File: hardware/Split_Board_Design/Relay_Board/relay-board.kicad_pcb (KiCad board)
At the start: 4 copper layers, 100 x 60 mm, 19 parts, among them J5 XT60PW-M, J6 Conn_01x06, J7 XT60PW-M, Q7 MJD41CT4G, U13 LTV-356T, U8 HF116F-80/24-1HTF

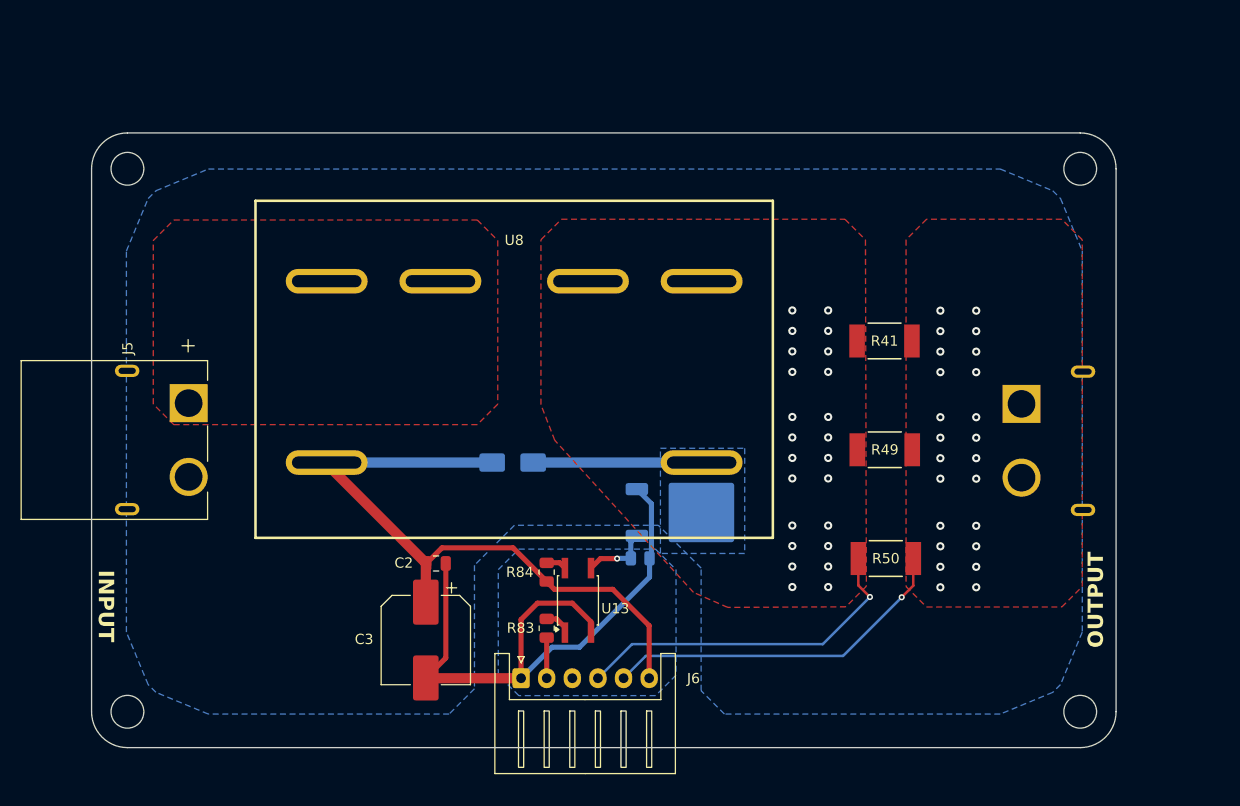
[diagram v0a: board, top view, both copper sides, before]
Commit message: feat(layout): Finish demo layout of relay board
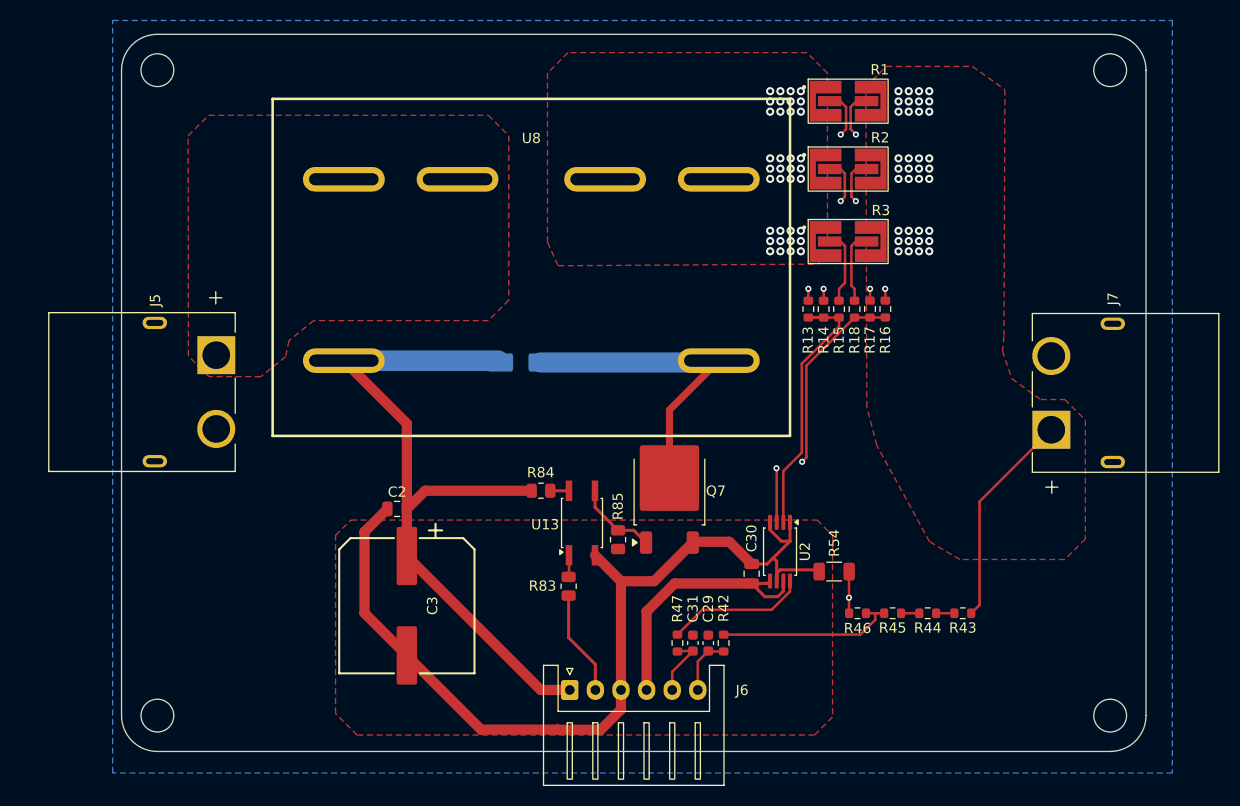
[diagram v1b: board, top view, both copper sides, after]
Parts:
- removed R41, R49, R50: 2mR, RobotChargeController:RES_1L00x_BRN
- added C29: 100nF-50V, Capacitor_SMD:C_0603_1608Metric, F.Cu at (158.3, 117.4)
- added C30: 100nF, Capacitor_SMD:C_0805_2012Metric, F.Cu at (162.5, 110.7)
- added C31: 10nF-50V, Capacitor_SMD:C_0603_1608Metric, F.Cu at (156.8, 117.4)
- added R1: 2mR, RobotChargeController:R_Shunt_FOJAN_2512L_4Terminal_Kelvin_C, F.Cu at (171.9, 64.5)
- added R13: 1R, Resistor_SMD:R_0603_1608Metric, F.Cu at (168.0, 84.8)
- added R14: 1R, Resistor_SMD:R_0603_1608Metric, F.Cu at (169.5, 84.8)
- added R15: 1R, Resistor_SMD:R_0603_1608Metric, F.Cu at (171.0, 84.8)
- added R16: 1R, Resistor_SMD:R_0603_1608Metric, F.Cu at (175.6, 84.8)
- added R17: 1R, Resistor_SMD:R_0603_1608Metric, F.Cu at (174.1, 84.8)
- added R18: 1R, Resistor_SMD:R_0603_1608Metric, F.Cu at (172.6, 84.8)
- added R2: 2mR, RobotChargeController:R_Shunt_FOJAN_2512L_4Terminal_Kelvin_C, F.Cu at (171.9, 71.2)
- added R3: 2mR, RobotChargeController:R_Shunt_FOJAN_2512L_4Terminal_Kelvin_C, F.Cu at (171.9, 78.2)
- added R42: 10kR, Resistor_SMD:R_0603_1608Metric, F.Cu at (159.8, 117.4)
- added R43: 150kR, Resistor_SMD:R_0603_1608Metric, F.Cu at (183.1, 114.5)
- added R44: 150kR, Resistor_SMD:R_0603_1608Metric, F.Cu at (179.7, 114.5)
- added R45: 150kR, Resistor_SMD:R_0603_1608Metric, F.Cu at (176.3, 114.5)
- added R46: 18kR, Resistor_SMD:R_0603_1608Metric, F.Cu at (172.8, 114.5)
- added R47: 1kR, Resistor_SMD:R_0603_1608Metric, F.Cu at (155.3, 117.4)
- added R54: 0R, Resistor_SMD:R_1206_3216Metric, F.Cu at (170.6, 110.4)
- added U2: INA240A2PW, Package_SO:TSSOP-8_4.4x3mm_P0.65mm, F.Cu at (165.3, 108.5)
- C3: value 100uF-50V -> 680uf-35v; footprint Capacitor_SMD:CP_Elec_8x10.5 -> RobotChargeController:CP_Elec_12.5x13.5_Generic_H13
- J7, Q7, R85: moved to F.Cu
- moved H4 109.8 mm to (197.5, 124.5)
- moved H5 90.6 mm to (104.5, 61.5)
- moved H6 62.7 mm to (197.5, 61.5)
- moved U8 10.1 mm to (141.0, 81.0)
- moved D7 9.80 mm to (140.0, 90.0)
- moved R84 7.97 mm to (141.9, 102.5), turned to 180 degrees
- moved U13 7.56 mm to (145.9, 105.7)
- moved C2 6.54 mm to (127.9, 104.3), turned to 180 degrees
- moved J7 5.50 mm to (197.8, 93.0), turned to 90 degrees
- moved J5 5.40 mm to (104.2, 92.9)
- moved J6 4.89 mm to (144.8, 122.0)
- moved R83 4.63 mm to (144.6, 111.9)
- moved C3 3.83 mm to (128.8, 113.8)
- moved H7 2.95 mm to (104.5, 124.5)
- moved R85 2.83 mm to (149.5, 107.3), turned to 90 degrees
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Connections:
- J6 pad 1: GND -> +24V
- J6 pad 3: 60V_GND -> GND
- J6 pad 4: /Relay_control/VBAT_RELAY_OUT_P -> +3V3
- J6 pad 5: Net-(J6-Pin_5) -> /Output_Sensing/IOUT_SENSE_ADC
- J6 pad 6: +24V -> /Output_Sensing/VOUT_SENSE_ADC
- J7 pad 1: Net-(J6-Pin_5) -> /Output_Sensing/VBAT_SEN_OUT_P
- U8 pad 6: /Relay_control/VBAT_RELAY_OUT_P -> /Output_Sensing/VBAT_RELAY_OUT_P
- U8 pad 8: /Relay_control/VBAT_RELAY_OUT_P -> /Output_Sensing/VBAT_RELAY_OUT_P
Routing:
- net /Relay_control/VBAT_RELAY_OUT_P: track 45.2 -> 0.00 mm, vias 25 -> 0
- net Net-(J6-Pin_5): track 34.7 -> 0.00 mm, vias 25 -> 0
- net GND: track 62.2 -> 90.2 mm
- net Net-(U2--): track 0.00 -> 27.3 mm, vias 0 -> 2
- net Net-(U2-+): track 0.00 -> 26.7 mm
- net +3V3: track 0.00 -> 25.8 mm
- net Net-(R1-V_A): track 0.00 -> 22.2 mm, vias 0 -> 2
- net Net-(R1-V_B): track 0.00 -> 22.1 mm, vias 0 -> 2
- net /Output_Sensing/VBAT_SEN_OUT_P: track 0.00 -> 21.2 mm, vias 0 -> 36
- net Net-(R42-Pad2): track 0.00 -> 17.8 mm
- net Net-(R2-V_A): track 0.00 -> 15.2 mm, vias 0 -> 2
- net Net-(R2-V_B): track 0.00 -> 15.1 mm, vias 0 -> 2
- net Net-(D7-A): track 16.4 -> 30.9 mm
- net Net-(R47-Pad2): track 0.00 -> 13.7 mm
- net Net-(R3-V_A): track 0.00 -> 7.20 mm
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- added copper zone on F.Cu, net /Output_Sensing/VBAT_RELAY_OUT_P
- added copper zone on In2.Cu, net /Output_Sensing/VBAT_RELAY_OUT_P
- added copper zone on F.Cu, net /Output_Sensing/VBAT_SEN_OUT_P
- added copper zone on In2.Cu, net /Output_Sensing/VBAT_SEN_OUT_P
- added copper zone on F.Cu, net GND
- removed copper zone on F.Cu, net /Relay_control/VBAT_RELAY_OUT_P
- removed copper zone on In2.Cu, net /Relay_control/VBAT_RELAY_OUT_P
- removed copper zone on B.Cu, net GND
- removed copper zone on B.Cu, net Net-(D7-A)
- removed copper zone on F.Cu, net Net-(J6-Pin_5)
- removed copper zone on In2.Cu, net Net-(J6-Pin_5)
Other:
- board size 100 x 60 mm -> 100 x 70 mm
- board text added: "{ "ViaStitching": "0.3.0", "stitch_zone_0": { "HSpacing": "1", "VSpacing": "1", "HOffset": "0", "VOffset": "0", "Clearance": "0.5", "Randomize": false, "Stagger": false, "OnlyFilledCopper": true } }"
- board text removed: "INPUT"
- board text removed: "OUTPUT"

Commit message: delete junk files
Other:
- board text added: "INPUT"
- board text added: "OUTPUT"

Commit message: feat(layout): Update layout
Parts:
- removed R13, R14, R15, R16, R17, R18: 1R, Resistor_SMD:R_0603_1608Metric
- C30: value 100nF -> 100nF-50V
- moved C3 4.98 mm to (133.6, 115.3), turned to 0 degrees
- moved R83 4.08 mm to (144.6, 115.9)
- moved R84 4.08 mm to (141.9, 106.6)
- moved U13 4.08 mm to (145.9, 109.8)
- moved C2 3.49 mm to (129.7, 107.3), turned to 0 degrees
- moved R3 2.40 mm to (171.9, 75.8)
- moved R1 1.95 mm to (172.0, 66.5)
- moved R85 0.28 mm to (149.4, 107.0)
- moved U2 0.15 mm to (165.3, 108.7)
- moved C30 0.09 mm to (162.4, 110.6)
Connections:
- R1 pad 3: Net-(R1-V_A) -> /Output_Sensing/VBAT_RELAY_OUT_P
- R1 pad 4: Net-(R1-V_B) -> /Output_Sensing/VBAT_SEN_OUT_P
- R2 pad 3: Net-(R2-V_A) -> /Output_Sensing/VBAT_RELAY_OUT_P
- R2 pad 4: Net-(R2-V_B) -> /Output_Sensing/VBAT_SEN_OUT_P
- R3 pad 3: Net-(R3-V_A) -> /Output_Sensing/VBAT_RELAY_OUT_P
- R3 pad 4: Net-(R3-V_B) -> /Output_Sensing/VBAT_SEN_OUT_P
- U2 pad 2: Net-(U2-+) -> /Output_Sensing/VBAT_RELAY_OUT_P
- U2 pad 3: Net-(U2--) -> /Output_Sensing/VBAT_SEN_OUT_P
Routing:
- net GND: track 90.2 -> 0.00 mm
- net /Output_Sensing/VBAT_SEN_OUT_P: track 21.2 -> 61.2 mm, vias 36 -> 38
- net /Output_Sensing/VBAT_RELAY_OUT_P: track 0.00 -> 38.4 mm
- net Net-(U2--): track 27.3 -> 0.00 mm, vias 2 -> 0
- net Net-(U2-+): track 26.7 -> 0.00 mm
- net Net-(R1-V_A): track 22.2 -> 0.00 mm, vias 2 -> 0
- net Net-(R1-V_B): track 22.1 -> 0.00 mm, vias 2 -> 0
- net Net-(R2-V_A): track 15.2 -> 0.00 mm, vias 2 -> 0
- net Net-(R2-V_B): track 15.1 -> 0.00 mm, vias 2 -> 0
- net Net-(R3-V_A): track 7.20 -> 0.00 mm
- net Net-(R3-V_B): track 7.11 -> 0.00 mm
- net +24V: track 71.2 -> 76.9 mm
- net /Relay_control/MAIN_RELAY_EN: track 10.3 -> 6.23 mm
- net Net-(Q7-B): track 8.03 -> 5.83 mm
- net /Output_Sensing/IOUT_SENSE_ADC: track 6.17 -> 5.47 mm

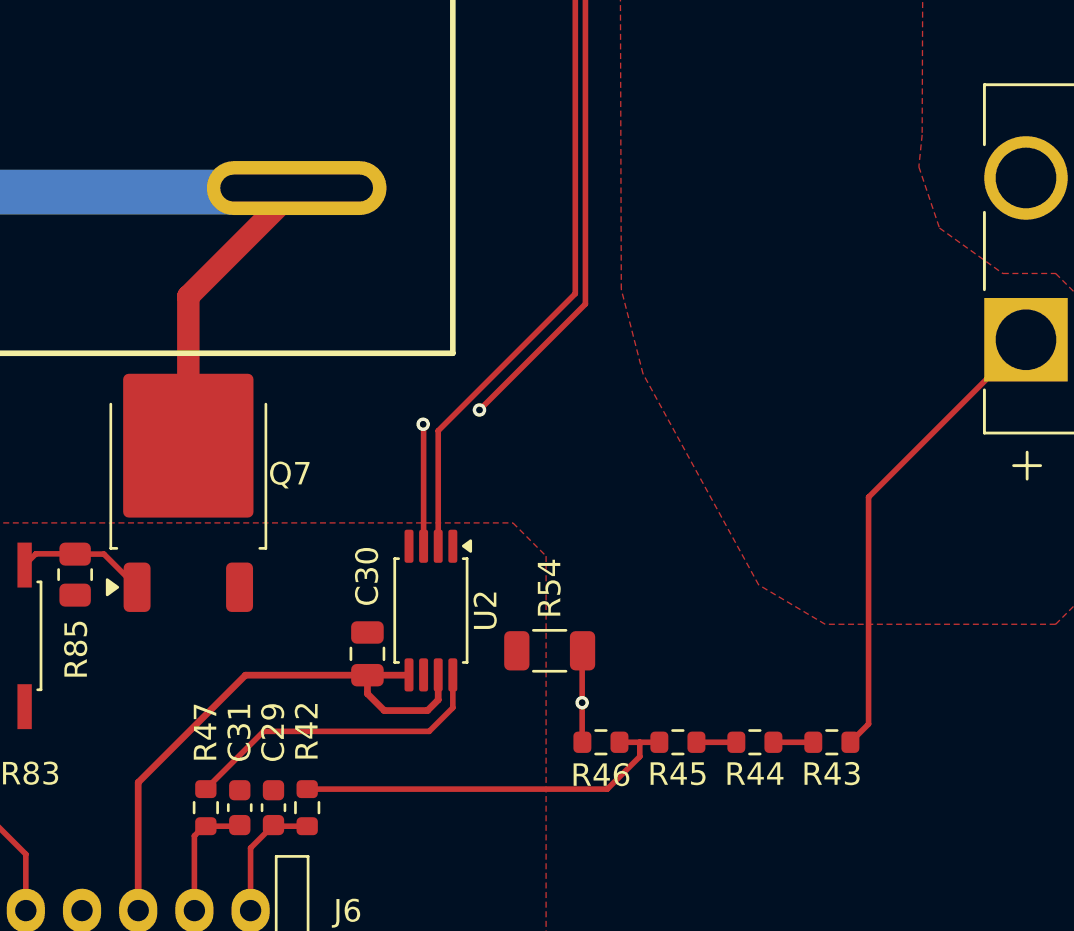
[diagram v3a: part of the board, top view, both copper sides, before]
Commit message: feat(schematic): update INA240A2PW to ÍNA240A2D
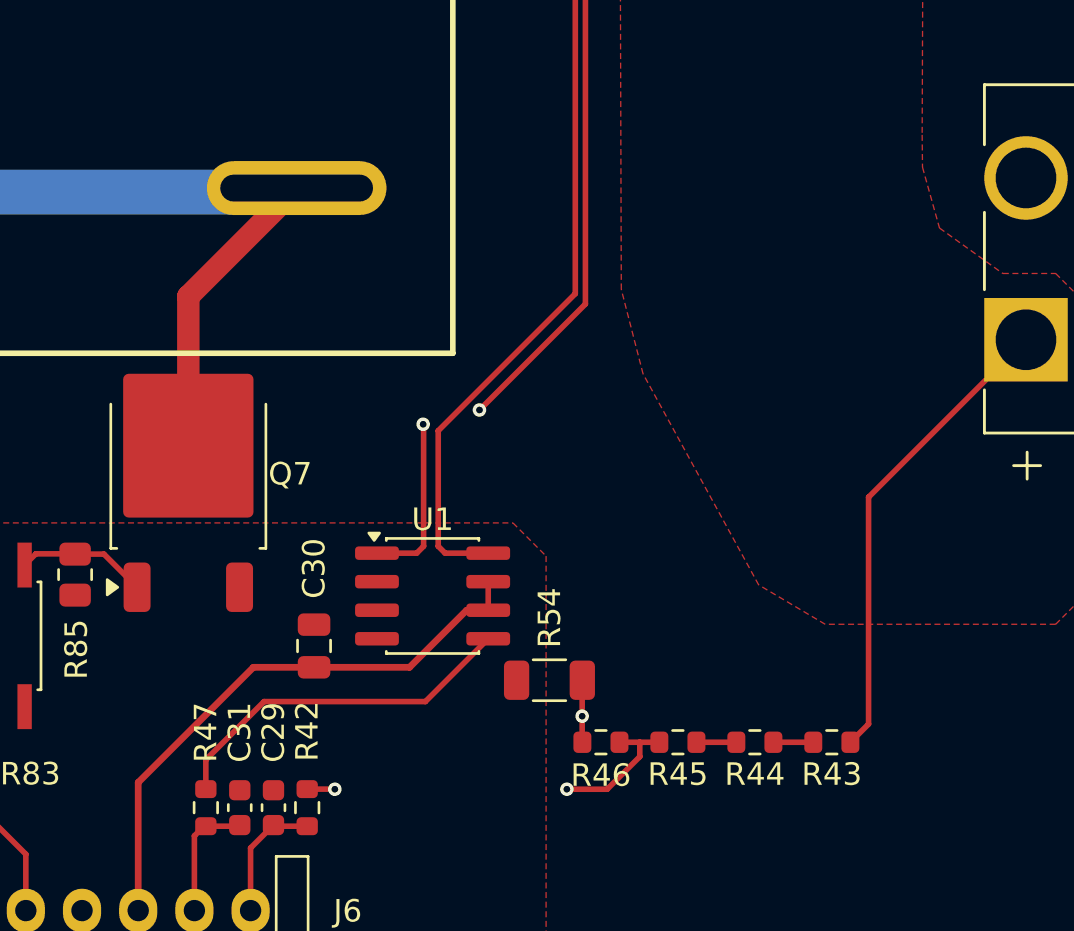
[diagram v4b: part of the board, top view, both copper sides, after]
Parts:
- removed U2: INA240A2PW, Package_SO:TSSOP-8_4.4x3mm_P0.65mm
- added U1: INA240A2D, Package_SO:SOIC-8_3.9x4.9mm_P1.27mm, F.Cu at (165.3, 108.0)
- moved C30 2.40 mm to (160.1, 110.2)
- moved R54 1.31 mm to (170.6, 111.8)
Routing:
- net /Output_Sensing/VBAT_RELAY_OUT_P: track 38.4 -> 40.8 mm
- net /Output_Sensing/VBAT_SEN_OUT_P: track 61.2 -> 63.4 mm
- net Net-(R47-Pad2): track 14.0 -> 16.1 mm
- net 60V_GND: track 4.08 -> 2.77 mm
- net Net-(R42-Pad2): vias 0 -> 2

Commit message: feat(layout): update relay board layout
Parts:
- removed C2: 100nF-50V, Capacitor_SMD:C_0805_2012Metric
- removed R1, R2, R3: 2mR, RobotChargeController:R_Shunt_FOJAN_2512L_4Terminal_Kelvin_C
- added J3: XT30PW-M, RobotChargeController:AMASS_XT30PW-M, F.Cu at (102.9, 109.5)
- added R48: 2mR, RobotChargeController:R_Shunt_FOJAN_2512L_4Terminal_Kelvin_C, F.Cu at (172.1, 66.4)
- added R49: 2mR, RobotChargeController:R_Shunt_FOJAN_2512L_4Terminal_Kelvin_C, F.Cu at (172.0, 71.2)
- added R50: 2mR, RobotChargeController:R_Shunt_FOJAN_2512L_4Terminal_Kelvin_C, F.Cu at (172.1, 75.8)
- C31: value 10nF-50V -> 100nF-50V
- R42: value 10kR -> 1kR
- moved C3 11.6 mm to (122.0, 116.8), turned to -90 degrees
- moved J5 9.83 mm to (104.3, 83.1)
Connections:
- J6 pad 1: +24V -> unconnected-(J6-Pin_1-Pad1)
- J6 pad 3: GND -> unconnected-(J6-Pin_3-Pad3)
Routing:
- net GND: track 0.00 -> 41.3 mm
- net +24V: track 76.9 -> 68.0 mm
- net /Output_Sensing/VBAT_RELAY_OUT_P: track 40.8 -> 41.3 mm
- added copper zone on In1.Cu, net /Output_Sensing/VBAT_RELAY_OUT_P
- added copper zone on In1.Cu, net /Output_Sensing/VBAT_SEN_OUT_P
- added copper zone on In1.Cu, net /Relay_control/VBAT_PROTECTED_P
- added copper zone on In2.Cu, net 60V_GND
- removed copper zone on In2.Cu, net /Output_Sensing/VBAT_RELAY_OUT_P
- removed copper zone on In2.Cu, net /Output_Sensing/VBAT_SEN_OUT_P
- removed copper zone on In2.Cu, net /Relay_control/VBAT_PROTECTED_P
- removed copper zone on In1.Cu, net 60V_GND

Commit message: layout: update layout
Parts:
- removed J3: XT30PW-M, RobotChargeController:AMASS_XT30PW-M
- added G***: LOGO, RobotChargeController:MSVN_LOGO, F.Cu at (177.8, 92.3)
- added J11: Conn_01x02, Connector_Phoenix_MC:PhoenixContact_MC_1,5_2-G-3.81_1x02_P3.81mm_Horizontal, F.Cu at (128.7, 121.3)
- moved C3 13.3 mm to (130.8, 106.8), turned to 180 degrees
- moved J5 9.83 mm to (103.9, 92.9)
- moved J6 2.00 mm to (144.8, 120.0)
- moved C29 1.97 mm to (158.2, 115.5)
- moved C31 1.97 mm to (156.8, 115.5)
- moved R47 1.97 mm to (155.2, 115.5)
- moved R83 1.50 mm to (146.0, 115.3), turned to 0 degrees
- moved R42 1.46 mm to (160.6, 116.2), turned to 0 degrees
- moved D7 0.18 mm to (140.0, 89.8)
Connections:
- J6 pad 1: unconnected-(J6-Pin_1-Pad1) -> GND
- J6 pad 3: unconnected-(J6-Pin_3-Pad3) -> GND
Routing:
- net GND: track 41.3 -> 17.2 mm
- net +24V: track 68.0 -> 57.2 mm
- net /Output_Sensing/VOUT_SENSE_ADC: track 5.75 -> 8.55 mm
- net Net-(R42-Pad2): track 17.8 -> 16.0 mm
- net Net-(R47-Pad2): track 16.1 -> 14.9 mm
- net /Relay_control/MAIN_RELAY_EN: track 6.23 -> 7.47 mm
- net +3V3: track 25.7 -> 26.3 mm
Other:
- board text added: "24V INPUT"
- board text added: "60V INPUT"
- board text added: "60V OUTPUT"
- board text added: "GND CTR GND 3V3 Io Vo"
- board text added: "ROBOT CHARGE CONTROLLER V1.0"
- board text removed: "INPUT"
- board text removed: "OUTPUT"
